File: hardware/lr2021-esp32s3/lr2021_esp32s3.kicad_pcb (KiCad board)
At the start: 4 copper layers, 90 x 65 mm, 84 parts, among them J1 USB-C, J2 5V IN, J3 3V3 IN, J4 GPIO, J5 SMA 915MHz, J6 SMA 2.4GHz, SW1 RESET, SW2 BOOT, U1 USBLC6-2SC6, U2 AP7361C-33E, U3 LM66100, U4 LM66100, U5 ESP32-S3-WROOM-1-N16R8, U6 LR2021IMLTRT, Y1 32MHz

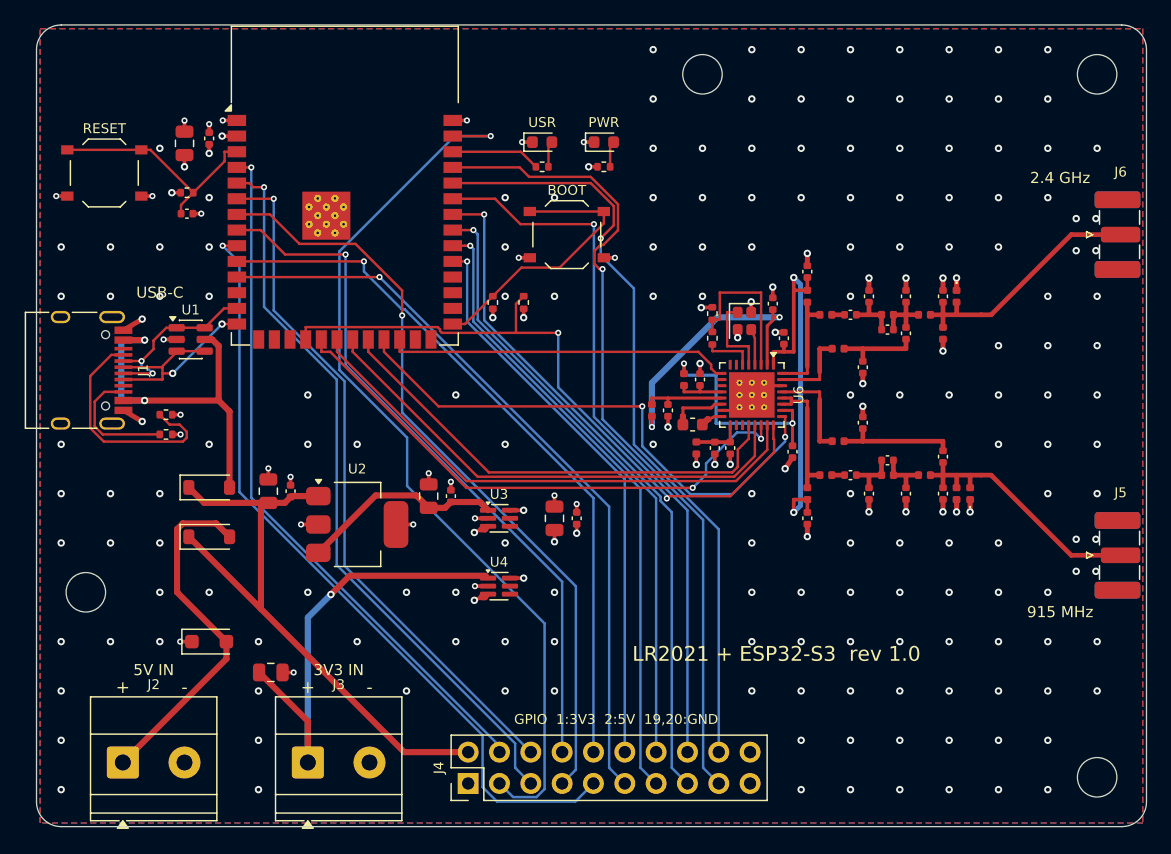
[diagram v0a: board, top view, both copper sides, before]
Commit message: Shrink the board from 90x65 mm to 64x52 mm
- Re-placed everything around the fixed constraints: ESP32 antenna at the
  top edge, LR2021 RF section and SMAs on the right, USB-C, terminals and
  GPIO header on the left/bottom edges
- Buttons rotated and moved next to the header; two M3 holes (right edge)
- GPIO header re-mapped to cut the routes crossing from the module's left
  side: now GPIO4-7, 9, 48, 38-42, 1 + UART, 3V3, 5V, 4x GND
  (GPIO15-18 no longer broken out)
- route.py keeps a 0.5 mm routing margin along the board edges
- ERC: 0 errors (intentional LM66100 OR warning); DRC with parity: 0 errors,
  0 unconnected; renders, drawings and fab outputs regenerated

Co-Authored-By: Claude Opus 5.5 <noreply@anthropic.com>
Claude-Session: https://claude.ai/code/session_01GybN5CQfdUnddB4A81xgKu
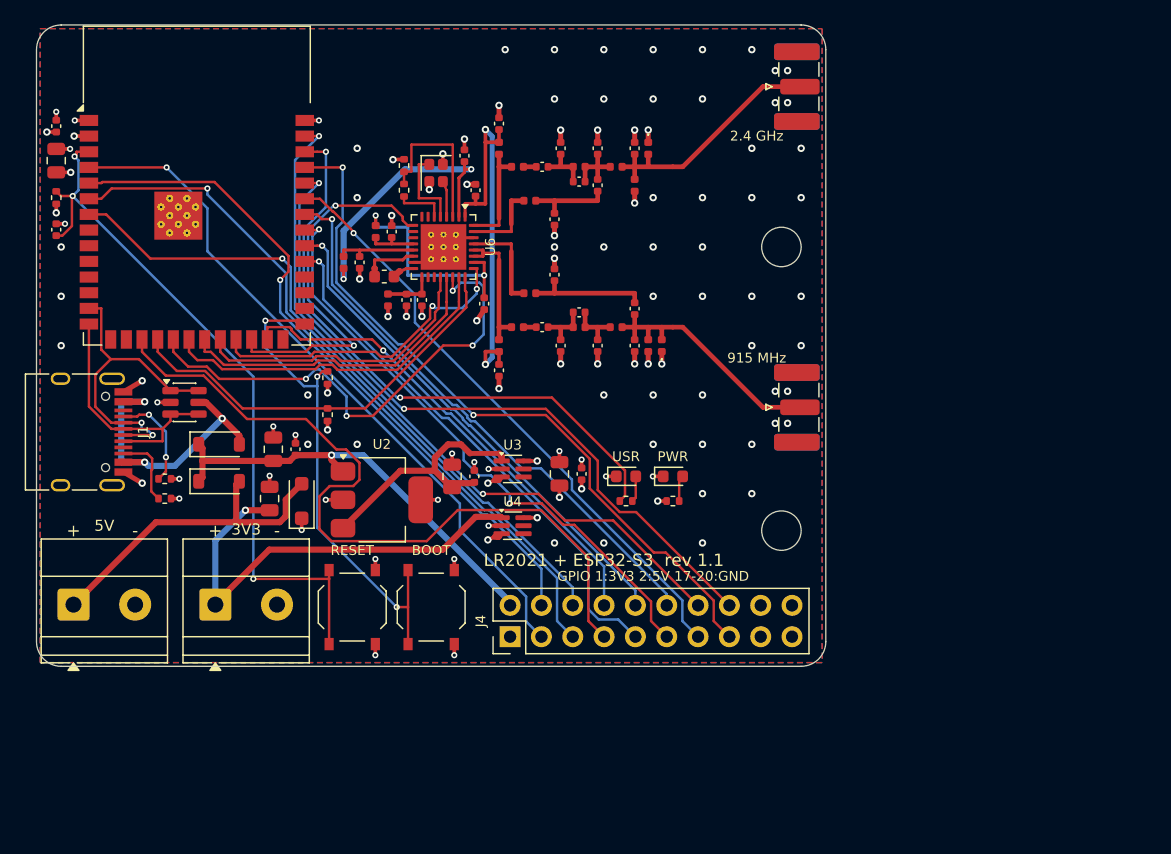
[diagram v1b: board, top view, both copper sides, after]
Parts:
- removed H3, H4: MountingHole, MountingHole:MountingHole_3.2mm_M3
- moved SW1 40.5 mm to (125.6, 147.2), turned to 90 degrees
- moved H2 32.5 mm to (160.4, 141.0)
- moved SW2 32.1 mm to (132.0, 147.2), turned to 90 degrees
- moved H1 29.2 mm to (160.4, 118.0)
- moved J5 28.6 mm to (161.9, 131.0)
- moved J6 28.6 mm to (161.9, 105.0)
- moved D5 27.9 mm to (147.8, 136.6)
- moved R6 27.9 mm to (147.8, 138.6)
- moved C11 27.7 mm to (131.2, 122.3)
- moved C12 27.7 mm to (130.0, 122.3)
- moved C21 27.7 mm to (144.0, 123.3)
- moved FB1 27.7 mm to (128.5, 122.3)
- moved C13 27.7 mm to (128.8, 116.8)
- moved C14 27.7 mm to (136.3, 122.6)
- moved C16 27.7 mm to (134.7, 110.6)
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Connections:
- J4 pad 10: /GPIO17 -> /GPIO39
- J4 pad 11: /GPIO18 -> /GPIO40
- J4 pad 12: /GPIO38 -> /GPIO41
- J4 pad 13: /GPIO39 -> /GPIO42
- J4 pad 14: /GPIO40 -> /GPIO1
- J4 pad 15: /GPIO41 -> /U0TXD
- J4 pad 16: /GPIO42 -> /U0RXD
- J4 pad 17: /U0TXD -> GND
- J4 pad 18: /U0RXD -> GND
- J4 pad 3: /GPIO1 -> /GPIO4
- J4 pad 4: /GPIO4 -> /GPIO5
- J4 pad 5: /GPIO5 -> /GPIO6
- J4 pad 6: /GPIO6 -> /GPIO7
- J4 pad 7: /GPIO7 -> /GPIO9
- J4 pad 8: /GPIO15 -> /GPIO48
- J4 pad 9: /GPIO16 -> /GPIO38
- U5 pad 10: /GPIO17 -> unconnected-(U5-IO17-Pad10)
- U5 pad 11: /GPIO18 -> unconnected-(U5-IO18-Pad11)
- U5 pad 17: unconnected-(U5-IO9-Pad17) -> /GPIO9
- U5 pad 25: unconnected-(U5-IO48-Pad25) -> /GPIO48
- U5 pad 8: /GPIO15 -> unconnected-(U5-IO15-Pad8)
- U5 pad 9: /GPIO16 -> unconnected-(U5-IO16-Pad9)
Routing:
- net /GPIO16: track 63.9 -> 0.00 mm, vias 1 -> 0
- net /GPIO9: track 0.00 -> 62.0 mm
- net /GPIO18: track 60.9 -> 0.00 mm, vias 1 -> 0
- net /GPIO17: track 57.9 -> 0.00 mm, vias 1 -> 0
- net /GPIO15: track 57.3 -> 0.00 mm, vias 1 -> 0
- net /LED_USER: track 7.25 -> 49.1 mm, vias 0 -> 2
- net /ESP_EN: track 19.1 -> 59.8 mm, vias 0 -> 3
- net /GPIO48: track 0.00 -> 39.6 mm, vias 0 -> 1
- net /LR_NSS: track 54.5 -> 33.8 mm, vias 2 -> 0
- net /LR_BUSY: track 44.2 -> 26.0 mm
- net /BOOT: track 22.6 -> 40.3 mm, vias 0 -> 3
- net /GPIO1: track 74.1 -> 58.6 mm, vias 1 -> 2
- net /LR_NRESET: track 38.9 -> 24.0 mm
- net /LR_MISO: track 41.0 -> 26.1 mm
- net /LR_SCK: track 43.3 -> 28.4 mm
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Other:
- board size 90 x 65 mm -> 64 x 52 mm
- board text added: "3V3"
- board text added: "5V"
- board text added: "GPIO 1:3V3 2:5V 17-20:GND"
- board text added: "LR2021 + ESP32-S3 rev 1.1"
- board text removed: "3V3 IN"
- board text removed: "5V IN"
- board text removed: "GPIO 1:3V3 2:5V 19,20:GND"
- board text removed: "LR2021 + ESP32-S3 rev 1.0"
- board text removed: "USB-C"

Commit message: Route the 62x47 mm WROOM-1U board; regenerate fab outputs and images
DRC with schematic parity: 0 errors, 0 unconnected, 0 mismatches.

Co-Authored-By: Claude Opus 5.5 <noreply@anthropic.com>
Claude-Session: https://claude.ai/code/session_01GybN5CQfdUnddB4A81xgKu
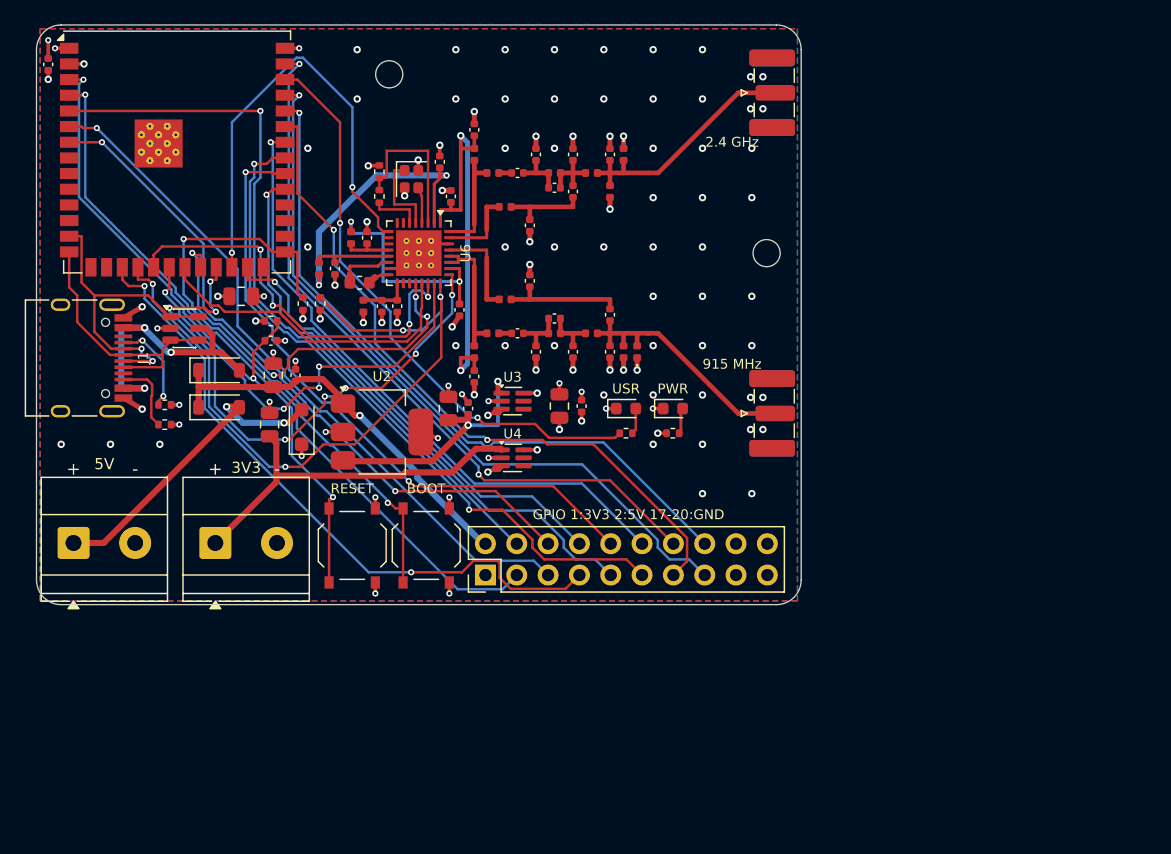
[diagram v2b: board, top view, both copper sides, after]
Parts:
- H1, H2: footprint MountingHole:MountingHole_3.2mm_M3 -> MountingHole:MountingHole_2.2mm_M2
- U5: value ESP32-S3-WROOM-1-N16R8 -> ESP32-S3-WROOM-1U-N16R8; footprint RF_Module:ESP32-S3-WROOM-1 -> RF_Module:ESP32-S3-WROOM-1U
- moved H2 48.8 mm to (128.6, 104.0)
- moved R4 20.1 mm to (119.0, 124.0), turned to 0 degrees
- moved C8 19.6 mm to (119.0, 125.6), turned to 0 degrees
- moved C9 18.6 mm to (116.6, 122.0), turned to 0 degrees
- moved R7 9.02 mm to (123.0, 122.6)
- moved R5 6.32 mm to (121.6, 122.6)
- moved C1 6.00 mm to (119.2, 128.4)
- moved C2 6.00 mm to (121.0, 128.4)
- moved C5 6.00 mm to (118.9, 132.4)
- moved D1 6.00 mm to (114.8, 128.0)
- moved D2 6.00 mm to (114.8, 131.0)
- moved D3 6.00 mm to (121.5, 132.6)
- moved J1 6.00 mm to (103.0, 127.0)
- moved R1 6.00 mm to (110.4, 130.8)
- moved R2 6.00 mm to (110.4, 132.4)
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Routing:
- net /LR_NSS: track 33.8 -> 57.5 mm, vias 0 -> 4
- net /LR_BUSY: track 26.0 -> 46.1 mm, vias 2 -> 8
- net /GPIO39: track 41.3 -> 52.6 mm, vias 1 -> 2
- net /BOOT: track 40.3 -> 49.9 mm, vias 3 -> 2
- net /LR_NRESET: track 24.0 -> 33.5 mm, vias 0 -> 4
- net /GPIO9: track 62.0 -> 53.3 mm, vias 0 -> 2
- net /LR_SCK: track 28.4 -> 35.9 mm, vias 0 -> 4
- net /LR_MOSI: track 40.5 -> 33.3 mm
- net /GPIO42: track 49.5 -> 56.5 mm, vias 1 -> 2
- net /+3V3_EXT: track 36.9 -> 30.1 mm, vias 1 -> 0
- net /GPIO40: track 49.0 -> 55.5 mm
- net /LR_DIO9: track 30.5 -> 36.9 mm
- net /GPIO41: track 46.2 -> 51.3 mm
- net /GPIO38: track 43.4 -> 47.7 mm
- net /GPIO5: track 56.3 -> 60.3 mm
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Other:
- board size 64 x 52 mm -> 62 x 47 mm
- board text added: "LR2021 + ESP32-S3 rev 1.2"
- board text removed: "LR2021 + ESP32-S3 rev 1.1"

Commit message: Fill in LCSC numbers for every BOM part; switch LEDs to AlInGaP
Stock checked in JLCPCB's parts search. The LR2021 (C49421489) is listed
but out of stock, so it needs Global Sourcing or consignment. Blue/InGaN
LEDs would barely light through 1k on 3.3V; USR is now red.

Co-Authored-By: Claude Opus 5.5 <noreply@anthropic.com>
Claude-Session: https://claude.ai/code/session_01GybN5CQfdUnddB4A81xgKu
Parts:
- D5: value BLUE -> RED
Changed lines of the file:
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@@
 			)
 		)
-		(property "Value" "BLUE"
+		(property "Value" "RED"
 			(at 0 1.43 0)
 			(layer "F.Fab")

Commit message: Route the reworked power section; pre-production check report
All eight check groups pass on the final board (see README, Pre-production
checks). Fab outputs, CPL with JLC corrections and images regenerated.

Co-Authored-By: Claude Opus 5.5 <noreply@anthropic.com>
Claude-Session: https://claude.ai/code/session_01GybN5CQfdUnddB4A81xgKu
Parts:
- C2: value 100nF -> 1uF
- moved C2 14.2 mm to (133.4, 135.3), turned to 0 degrees
- turned U2 to 180 degrees
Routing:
- net /LR_NSS: track 57.5 -> 36.0 mm, vias 4 -> 2
- net /LR_DIO9: track 36.9 -> 17.6 mm
- net /LR_BUSY: track 46.1 -> 27.4 mm, vias 8 -> 0
- net /BOOT: track 49.9 -> 36.8 mm, vias 2 -> 3
- net /LR_SCK: track 35.9 -> 48.1 mm, vias 4 -> 6
- net /GPIO40: track 55.5 -> 66.2 mm, vias 2 -> 3
- net /LR_NRESET: track 33.5 -> 43.7 mm, vias 4 -> 6
- net /U0TXD: track 59.8 -> 69.7 mm, vias 1 -> 2
- net /U0RXD: track 56.5 -> 65.3 mm, vias 1 -> 3
- net /+3V3_LDO: track 21.1 -> 12.5 mm
- net /GPIO39: track 52.6 -> 44.3 mm, vias 2 -> 1
- net /USB_DN: track 26.7 -> 34.1 mm
- net /GPIO48: track 37.7 -> 44.5 mm, vias 1 -> 2
- net /GPIO7: track 55.7 -> 62.2 mm, vias 2 -> 1
- net /GPIO6: track 56.9 -> 62.9 mm, vias 1 -> 2
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
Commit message: Design review round 4: antenna ESD diodes and RF via fence
Full pre-production review with simulations (docs/design_review.md,
scripts in analysis/):
- ngspice power-path model: USB plug-in, LoRa TX + Wi-Fi droop,
  inrush and source switchover
- nodal RF model of both matching networks built from the netlist,
  and a graph comparison against Semtech's e788v01a reference
- thermal, current capacity and assembly spacing checks

Fixes:
- D6/D7 antenna ESD diodes are now fitted (DOWO PESD0402V12,
  C19626255, 0.05 pF, 12 V), as in the reference design
- add_rf_fence.py adds a 32-via GND fence along both antenna feeds
  after routing; build.py runs it and re-checks DRC

Fab files regenerated: Gerbers/drill (271 PTH), BOM and CPL.

Co-Authored-By: Claude Opus 5.5 <noreply@anthropic.com>
Claude-Session: https://claude.ai/code/session_01GybN5CQfdUnddB4A81xgKu
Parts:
- D6, D7: value ESD101-B1-02ELS -> PESD0402V12
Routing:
- net GND: vias 107 -> 139
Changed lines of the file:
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@@
 			)
 		)
-		(property "Value" "ESD101-B1-02ELS"
+		(property "Value" "PESD0402V12"
 			(at 0 1.17 270)
 			(layer "F.Fab")
@@
 		)
 		(sheetfile "lr2021_esp32s3.kicad_sch")
-		(attr smd dnp)
+		(attr smd)
 		(fp_circle
 			(center -1.09 0)
@@
 		)
 		(embedded_fonts no)
-		(model "${KICAD9_3DMODEL_DIR}/Diode_SMD.3dshapes/D_0402_1005Metric.step"
+		(model "${KIPRJMOD}/lib/3d/D_0402_1005Metric.step"
 			(offset
 				(xyz 0 0 0)
@@
 			)
 		)
-		(property "Value" "ESD101-B1-02ELS"
+		(property "Value" "PESD0402V12"
 			(at 0 1.17 90)
 			(layer "F.Fab")
@@
 		)
 		(sheetfile "lr2021_esp32s3.kicad_sch")
-		(attr smd dnp)
+		(attr smd)
 		(fp_circle
 			(center -1.09 0)
@@
 		)
 		(embedded_fonts no)
-		(model "${KICAD9_3DMODEL_DIR}/Diode_SMD.3dshapes/D_0402_1005Metric.step"
+		(model "${KIPRJMOD}/lib/3d/D_0402_1005Metric.step"
 			(offset
 				(xyz 0 0 0)
@@
 	)
 	(via
+		(at 151.071751 124.328248)
+		(size 0.5)
+		(drill 0.25)
+		(layers "F.Cu" "B.Cu")
+		(net 62)
+	)
+	(via
 		(at 129.25 124.13)
 		(size 0.6)
@@
 	)
 	(via
+		(at 153.671751 126.928248)
+		(size 0.5)
+		(drill 0.25)
+		(layers "F.Cu" "B.Cu")
+		(net 62)
+	)
+	(via
 		(at 154 134)
 		(size 0.6)
@@
 	)
 	(via
+		(at 149.6 111.05)
+		(size 0.5)
+		(drill 0.25)
+		(layers "F.Cu" "B.Cu")
+		(net 62)
+	)
+	(via
+		(at 156.271751 107.471751)
+		(size 0.5)
+		(drill 0.25)
+		(layers "F.Cu" "B.Cu")
+		(net 62)
+	)
+	(via
 		(at 111.58 130.8)
 		(size 0.5)
@@
 	)
 	(via
+		(at 152.371751 111.371751)
+		(size 0.5)
+		(drill 0.25)
+		(layers "F.Cu" "B.Cu")
+		(net 62)
+	)
+	(via
+		(at 152.371751 125.628248)
+		(size 0.5)
+		(drill 0.25)
+		(layers "F.Cu" "B.Cu")
+		(net 62)
+	)
+	(via
 		(at 158 122)
 		(size 0.6)
@@
 	)
 	(via
+		(at 154.928248 130.871751)
+		(size 0.5)
+		(drill 0.25)
+		(layers "F.Cu" "B.Cu")
+		(net 62)
+	)
+	(via
 		(at 154 114)
 		(size 0.6)
@@
 	)
 	(via
+		(at 145.55 126.02)
+		(size 0.5)
+		(drill 0.25)
+		(layers "F.Cu" "B.Cu")
+		(net 62)
+	)
+	(via
 		(at 142 118)
 		(size 0.6)
@@
 	)
 	(via
+		(at 152.328248 108.728248)
+		(size 0.5)
+		(drill 0.25)
+		(layers "F.Cu" "B.Cu")
+		(net 62)
+	)
+	(via
 		(at 133.7 124.48)
 		(size 0.6)
@@
 	)
 	(via
+		(at 145.55 110.98)
+		(size 0.5)
+		(drill 0.25)
+		(layers "F.Cu" "B.Cu")
+		(net 62)
+	)
+	(via
 		(at 157.9 130.199999)
 		(size 0.6)
@@
 	)
 	(via
+		(at 151.071751 112.671751)
+		(size 0.5)
+		(drill 0.25)
+		(layers "F.Cu" "B.Cu")
+		(net 62)
+	)
+	(via
 		(at 158 138)
 		(size 0.6)
@@
 	)
 	(via
+		(at 151.028248 110.028248)
+		(size 0.5)
+		(drill 0.25)
+		(layers "F.Cu" "B.Cu")
+		(net 62)
+	)
+	(via
 		(at 136.65 135.1)
 		(size 0.5)
@@
 	)
 	(via
+		(at 156.271751 129.528248)
+		(size 0.5)
+		(drill 0.25)
+		(layers "F.Cu" "B.Cu")
+		(net 62)
+	)
+	(via
 		(at 150 114)
 		(size 0.6)
@@
 	)
 	(via
+		(at 149.6 124.05)
+		(size 0.5)
+		(drill 0.25)
+		(layers "F.Cu" "B.Cu")
+		(net 62)
+	)
+	(via
 		(at 126 110)
 		(size 0.6)
@@
 	)
 	(via
+		(at 156.9 132.449999)
+		(size 0.5)
+		(drill 0.25)
+		(layers "F.Cu" "B.Cu")
+		(net 62)
+	)
+	(via
+		(at 154.971751 108.771751)
+		(size 0.5)
+		(drill 0.25)
+		(layers "F.Cu" "B.Cu")
+		(net 62)
+	)
+	(via
+		(at 156.9 104.55)
+		(size 0.5)
+		(drill 0.25)
+		(layers "F.Cu" "B.Cu")
+		(net 62)
+	)
+	(via
+		(at 153.628248 107.428248)
+		(size 0.5)
+		(drill 0.25)
+		(layers "F.Cu" "B.Cu")
+		(net 62)
+	)
+	(via
 		(at 119.2 126.55)
 		(size 0.5)
@@
 	)
 	(via
+		(at 154.971751 128.228248)
+		(size 0.5)
+		(drill 0.25)
+		(layers "F.Cu" "B.Cu")
+		(net 62)
+	)
+	(via
 		(at 134 106)
 		(size 0.6)
@@
 	)
 	(via
+		(at 147.5425 124.05)
+		(size 0.5)
+		(drill 0.25)
+		(layers "F.Cu" "B.Cu")
+		(net 62)
+	)
+	(via
 		(at 134.609999 135.3)
 		(size 0.5)
@@
 	)
 	(via
+		(at 154.928248 106.128248)
+		(size 0.5)
+		(drill 0.25)
+		(layers "F.Cu" "B.Cu")
+		(net 62)
+	)
+	(via
 		(at 148.7 127.985)
 		(size 0.6)
@@
 	)
 	(via
+		(at 152.328248 128.271751)
+		(size 0.5)
+		(drill 0.25)
+		(layers "F.Cu" "B.Cu")
+		(net 62)
+	)
+	(via
 		(at 126 106)
 		(size 0.6)
@@
 	)
 	(via
+		(at 149.6 112.95)
+		(size 0.5)
+		(drill 0.25)
+		(layers "F.Cu" "B.Cu")
+		(net 62)
+	)
+	(via
+		(at 151.028248 126.971751)
+		(size 0.5)
+		(drill 0.25)
+		(layers "F.Cu" "B.Cu")
+		(net 62)
+	)
+	(via
+		(at 147.45 113.015)
+		(size 0.5)
+		(drill 0.25)
+		(layers "F.Cu" "B.Cu")
+		(net 62)
+	)
+	(via
 		(at 142 110)
 		(size 0.6)
@@
 	)
 	(via
+		(at 145.55 113.015)
+		(size 0.5)
+		(drill 0.25)
+		(layers "F.Cu" "B.Cu")
+		(net 62)
+	)
+	(via
+		(at 148.549999 110.985)
+		(size 0.5)
+		(drill 0.25)
+		(layers "F.Cu" "B.Cu")
+		(net 62)
+	)
+	(via
+		(at 150.4 124.05)
+		(size 0.5)
+		(drill 0.25)
+		(layers "F.Cu" "B.Cu")
+		(net 62)
+	)
+	(via
 		(at 128 124.13)
 		(size 0.6)
@@
 	)
 	(via
+		(at 150.4 112.95)
+		(size 0.5)
+		(drill 0.25)
+		(layers "F.Cu" "B.Cu")
+		(net 62)
+	)
+	(via
 		(at 150 122)
 		(size 0.6)
@@
 	)
 	(via
+		(at 156.228248 104.828248)
+		(size 0.5)
+		(drill 0.25)
+		(layers "F.Cu" "B.Cu")
+		(net 62)
+	)
+	(via
+		(at 145.485 124.05)
+		(size 0.5)
+		(drill 0.25)
+		(layers "F.Cu" "B.Cu")
+		(net 62)
+	)
+	(via
 		(at 157.9 132.8)
 		(size 0.6)
@@
 		(layers "F.Cu" "B.Cu")
 		(net 62)
+	)
+	(via
+		(at 156.228248 132.171751)
+		(size 0.5)
+		(drill 0.25)
+		(layers "F.Cu" "B.Cu")
+		(net 62)
